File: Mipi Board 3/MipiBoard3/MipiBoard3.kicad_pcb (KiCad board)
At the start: 4 copper layers, 55 x 45 mm, 21 parts, among them J1 Power/Control Top, J2 Bank A Top, J3 Bank B Top, J4 MIPI1, J5 MIPI2, J6 Bank A Bottom, J7 Bank B Bottom, J8 Power/Control Bottom

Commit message: Components layedout
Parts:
- added C1: C, Capacitor_SMD:C_0201_0603Metric, F.Cu at (77.6, 60.2)
- added C2: C, Capacitor_SMD:C_0201_0603Metric, F.Cu at (77.7, 67.6)
- added C3: C, Capacitor_SMD:C_0201_0603Metric, F.Cu at (77.6, 75.0)
- added C4: C, Capacitor_SMD:C_0201_0603Metric, F.Cu at (65.6, 60.0)
- added R14: R, Resistor_SMD:R_0603_1608Metric, F.Cu at (65.6, 58.7)
- added R15: R, Resistor_SMD:R_0603_1608Metric, F.Cu at (62.4, 58.7)
- added R16: R, Resistor_SMD:R_0402_1005Metric, F.Cu at (71.4, 65.8)
- added R17: R, Resistor_SMD:R_0402_1005Metric, F.Cu at (72.3, 73.2)
- added R18: R, Resistor_SMD:R_0402_1005Metric, F.Cu at (71.8, 80.5)
- added R19: R, Resistor_SMD:R_0402_1005Metric, F.Cu at (83.4, 80.0)
- added R20: R, Resistor_SMD:R_0402_1005Metric, F.Cu at (83.8, 72.6)
- added R21: R, Resistor_SMD:R_0402_1005Metric, F.Cu at (83.3, 65.2)
- added R22: R, Resistor_SMD:R_0402_1005Metric, F.Cu at (71.4, 64.5)
- added R23: R, Resistor_SMD:R_0402_1005Metric, F.Cu at (72.3, 71.9)
- added R24: R, Resistor_SMD:R_0402_1005Metric, F.Cu at (71.8, 79.3)
- added R25: R, Resistor_SMD:R_0603_1608Metric, F.Cu at (84.9, 77.3)
- added R26: R, Resistor_SMD:R_0603_1608Metric, F.Cu at (84.9, 75.8)
- added R27: R, Resistor_SMD:R_0603_1608Metric, F.Cu at (84.9, 69.9)
- added R28: R, Resistor_SMD:R_0603_1608Metric, F.Cu at (84.9, 68.4)
- added R29: R, Resistor_SMD:R_0603_1608Metric, F.Cu at (71.6, 62.5)
- added R30: R, Resistor_SMD:R_0603_1608Metric, F.Cu at (71.6, 60.8)
- added R31: R, Resistor_SMD:R_0603_1608Metric, F.Cu at (84.2, 62.0)
- added R32: R, Resistor_SMD:R_0603_1608Metric, F.Cu at (84.2, 60.3)
- added R33: R, Resistor_SMD:R_0603_1608Metric, F.Cu at (70.8, 68.3)
- added R34: R, Resistor_SMD:R_0603_1608Metric, F.Cu at (70.8, 70.1)
- added R35: R, Resistor_SMD:R_0603_1608Metric, F.Cu at (71.2, 76.2)
- added R36: R, Resistor_SMD:R_0603_1608Metric, F.Cu at (71.2, 77.7)
- added U1: LM339, Package_SO:TSSOP-14-1EP_4.4x5mm_P0.65mm, F.Cu at (77.8, 63.9)
- added U2: LM339, Package_SO:TSSOP-14-1EP_4.4x5mm_P0.65mm, F.Cu at (77.9, 71.2)
- added U3: LM339, Package_SO:TSSOP-14-1EP_4.4x5mm_P0.65mm, F.Cu at (77.8, 78.7)
- moved R7 34.3 mm to (59.7, 67.0), turned to 90 degrees
- moved R10 32.9 mm to (59.7, 70.0), turned to 90 degrees
- moved R13 32.4 mm to (59.7, 73.1), turned to 90 degrees
- moved R12 11.3 mm to (83.3, 63.9)
- moved R2 10.7 mm to (60.7, 79.9), turned to -90 degrees
- moved R9 8.86 mm to (83.7, 71.2)
- moved R6 8.75 mm to (83.5, 78.8)
- moved R1 5.14 mm to (63.0, 79.9), turned to -90 degrees
- moved R3 4.40 mm to (92.3, 64.4)
- moved R4 3.60 mm to (94.8, 64.4)
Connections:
- J4 pad 10: GND -> 34_L5/1.5B_P
- J4 pad 11: GND -> 34_L5/1.5B_N
- J4 pad 13: GND -> 34_L1/1.5B_P
- J4 pad 14: GND -> 34_L1/1.5B_N
- J4 pad 7: GND -> 34_L3/1.5B_P
- J4 pad 8: GND -> 34_L3/1.5B_N
- J5 pad 10: 34_L5/1.5B_P -> 34_L8/1.5B_P
- J5 pad 11: 34_L5/1.5B_N -> 34_L8/1.5B_N
- J5 pad 13: 34_L9/1.5B_P -> 34_L7/1.5B_P
- J5 pad 14: 34_L9/1.5B_N -> 34_L7/1.5B_N
- J5 pad 7: 34_L6/1.5B_P -> 34_L9/1.5B_P
- J5 pad 8: 34_L6/1.5B_N -> 34_L9/1.5B_N
- R10 pad 1: 34_L7/1.5B_N -> 34_L5/1.5B_P
- R11 pad 1: 34_L6/1.5B_P -> 34_L9/1.5B_P
- R11 pad 2: 34_L6/1.5B_N -> 34_L9/1.5B_N
- R12 pad 1: 34_L4/1.5B_P -> Net-(U1C-+)
- R12 pad 2: 34_L6/1.5B_P -> 34_L9/1.5B_P
- R13 pad 1: 34_L4/1.5B_N -> 34_L3/1.5B_P
- R13 pad 2: 34_L6/1.5B_N -> 34_L3/1.5B_N
- R5 pad 1: 34_L9/1.5B_P -> 34_L7/1.5B_P
- R5 pad 2: 34_L9/1.5B_N -> 34_L7/1.5B_N
- R6 pad 1: 34_L8/1.5B_P -> Net-(U3C-+)
- R6 pad 2: 34_L9/1.5B_P -> 34_L7/1.5B_P
- R7 pad 1: 34_L8/1.5B_N -> 34_L1/1.5B_P
- R7 pad 2: 34_L9/1.5B_N -> 34_L1/1.5B_N
- R8 pad 1: 34_L5/1.5B_P -> 34_L8/1.5B_P
- R8 pad 2: 34_L5/1.5B_N -> 34_L8/1.5B_N
- R9 pad 1: 34_L7/1.5B_P -> Net-(U2C-+)
- R9 pad 2: 34_L5/1.5B_P -> 34_L8/1.5B_P
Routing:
- net +3V3: track 81.3 -> 10.0 mm
- net 14_L10_N/1.2C: track 40.3 -> 1.72 mm, vias 3 -> 1
- net 14_L10_P/1.2C: track 37.9 -> 0.00 mm, vias 2 -> 0
- net 14_L15_N/1.2C: track 37.6 -> 1.97 mm
- net 14_L22_N/1.2D: track 37.6 -> 2.20 mm
- net 14_L22_P/1.2D: track 36.8 -> 2.17 mm
- net 34_L7/1.5B_P: track 33.5 -> 0.00 mm, vias 1 -> 0
- net 34_L6/1.5B_P: track 33.6 -> 0.79 mm
- net 14_L16_P/1.2C: track 34.6 -> 1.79 mm, vias 2 -> 1
- net 34_L9/1.5B_N: track 31.9 -> 0.00 mm, vias 2 -> 0
- net 34_L5/1.5B_P: track 34.0 -> 2.77 mm, vias 2 -> 1
- net 34_L5/1.5B_N: track 33.2 -> 2.01 mm, vias 2 -> 1
- net 34_L7/1.5B_N: track 31.1 -> 0.00 mm, vias 1 -> 0
- net 14_L16_N/1.2C: track 32.8 -> 1.72 mm
- net 34_L8/1.5B_N: track 31.1 -> 0.00 mm, vias 1 -> 0
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
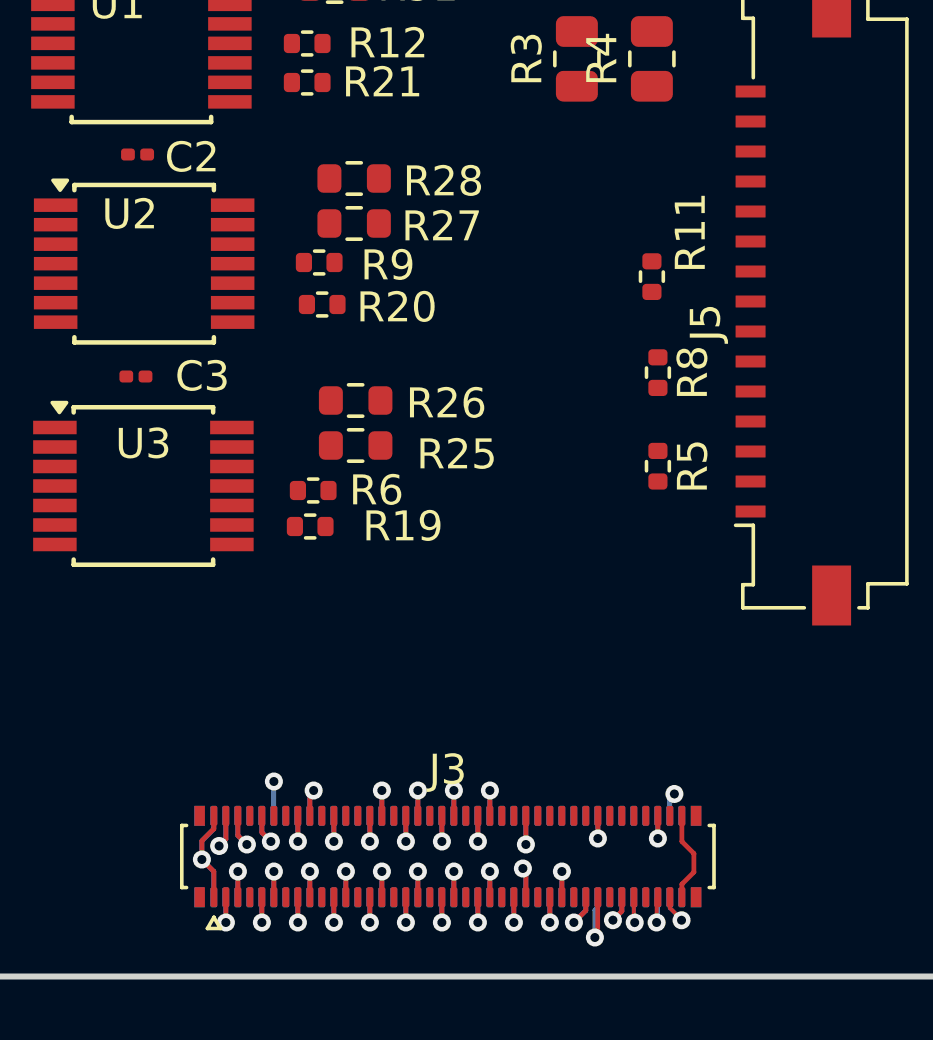
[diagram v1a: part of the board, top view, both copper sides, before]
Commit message: first few wires routed
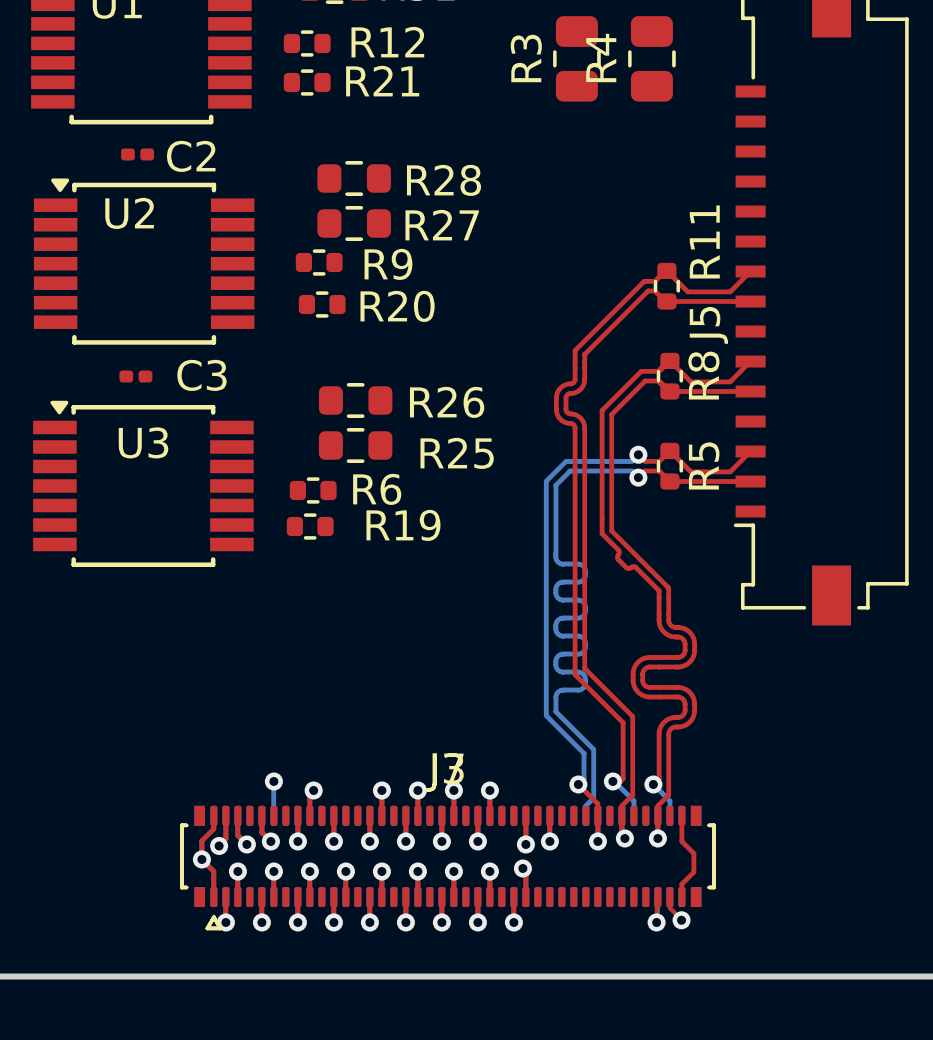
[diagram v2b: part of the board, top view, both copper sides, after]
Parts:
- moved R11 0.59 mm to (95.3, 72.0)
- moved R8 0.42 mm to (95.4, 75.0)
- moved R5 0.40 mm to (95.4, 78.0)
- moved J7 0.08 mm to (88.0, 91.0)
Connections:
- J4 pad 10: 34_L5/1.5B_P -> 34_L4/1.5B_P
- J4 pad 11: 34_L5/1.5B_N -> 34_L4/1.5B_N
- J4 pad 13: 34_L1/1.5B_P -> 34_L7/1.5B_P
- J4 pad 14: 34_L1/1.5B_N -> 34_L7/1.5B_N
- J5 pad 10: 34_L8/1.5B_P -> 34_L6/1.5B_P
- J5 pad 11: 34_L8/1.5B_N -> 34_L6/1.5B_N
- J5 pad 13: 34_L7/1.5B_P -> 34_L8/1.5B_P
- J5 pad 14: 34_L7/1.5B_N -> 34_L8/1.5B_N
- R10 pad 1: 34_L5/1.5B_P -> 34_L4/1.5B_P
- R10 pad 2: 34_L5/1.5B_N -> 34_L4/1.5B_N
- R16 pad 2: 34_L1/1.5B_P -> 34_L7/1.5B_P
- R17 pad 2: 34_L5/1.5B_P -> 34_L4/1.5B_P
- R19 pad 2: 34_L7/1.5B_N -> 34_L8/1.5B_N
- R20 pad 2: 34_L8/1.5B_N -> 34_L6/1.5B_N
- R22 pad 2: 34_L1/1.5B_N -> 34_L7/1.5B_N
- R23 pad 2: 34_L5/1.5B_N -> 34_L4/1.5B_N
- R5 pad 1: 34_L7/1.5B_P -> 34_L8/1.5B_P
- R5 pad 2: 34_L7/1.5B_N -> 34_L8/1.5B_N
- R6 pad 2: 34_L7/1.5B_P -> 34_L8/1.5B_P
- R7 pad 1: 34_L1/1.5B_P -> 34_L7/1.5B_P
- R7 pad 2: 34_L1/1.5B_N -> 34_L7/1.5B_N
- R8 pad 1: 34_L8/1.5B_P -> 34_L6/1.5B_P
- R8 pad 2: 34_L8/1.5B_N -> 34_L6/1.5B_N
- R9 pad 2: 34_L8/1.5B_P -> 34_L6/1.5B_P
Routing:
- net 34_L9/1.5B_N: track 0.00 -> 25.0 mm, vias 0 -> 1
- net 34_L9/1.5B_P: track 0.00 -> 25.0 mm, vias 0 -> 1
- net 34_L8/1.5B_N: track 0.00 -> 24.7 mm, vias 0 -> 1
- net 34_L6/1.5B_P: track 0.79 -> 25.2 mm
- net 34_L6/1.5B_N: track 1.52 -> 25.3 mm
- net 34_L8/1.5B_P: track 1.52 -> 21.7 mm, vias 1 -> 3
- net 34_L5/1.5B_P: track 2.77 -> 0.00 mm, vias 1 -> 0
- net 34_L5/1.5B_N: track 2.01 -> 0.00 mm, vias 1 -> 0
- net 34_L1_N/1.5A: track 1.78 -> 0.00 mm, vias 1 -> 0
- net 34_L3/1.5B_P: track 1.72 -> 0.00 mm, vias 1 -> 0
- net 34_L1_P/1.5A: track 1.72 -> 0.00 mm, vias 1 -> 0
- net 34_L7/1.5B_N: track 0.00 -> 1.72 mm, vias 0 -> 1
- net 34_L3/1.5B_N: track 1.68 -> 0.00 mm, vias 1 -> 0

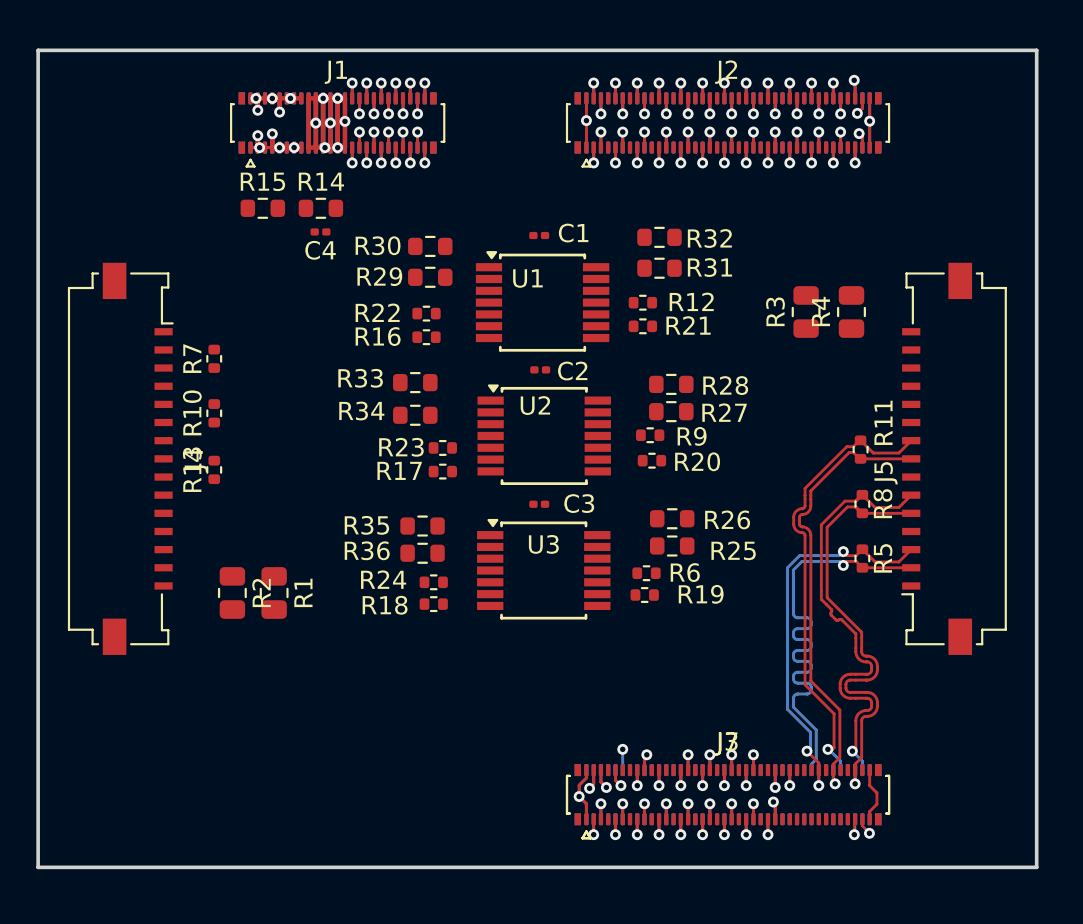
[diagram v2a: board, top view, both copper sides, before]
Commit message: length pairs matching
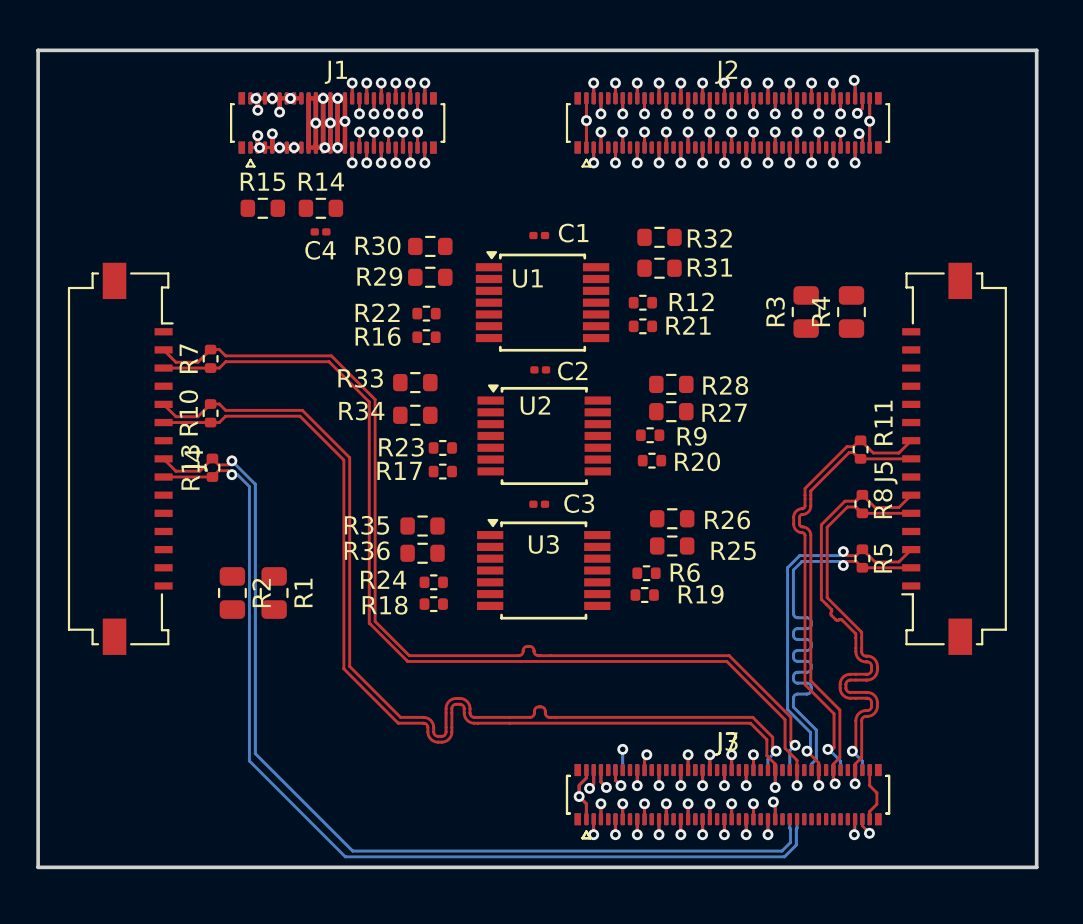
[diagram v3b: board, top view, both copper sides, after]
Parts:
- moved R10 0.20 mm to (59.5, 70.0)
- moved R7 0.20 mm to (59.5, 67.0)
- moved R13 0.16 mm to (59.6, 73.0)
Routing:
- net 34_L7/1.5B_P: track 0.00 -> 54.4 mm, vias 0 -> 1
- net 34_L3/1.5B_N: track 0.00 -> 54.4 mm, vias 0 -> 1
- net 34_L3/1.5B_P: track 0.00 -> 54.4 mm, vias 0 -> 1
- net 34_L4/1.5B_N: track 0.01 -> 54.3 mm, vias 0 -> 1
- net 34_L7/1.5B_N: track 1.72 -> 54.5 mm
- net 34_L4/1.5B_P: track 1.92 -> 54.3 mm

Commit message: better central wiring
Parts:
- moved R32 13.3 mm to (71.2, 62.7)
- moved R31 13.1 mm to (71.2, 61.1)
- moved R29 12.8 mm to (84.4, 62.6), turned to 180 degrees
- moved R30 12.7 mm to (84.3, 61.0), turned to 180 degrees
- moved R14 2.49 mm to (64.2, 60.8), turned to 90 degrees
- moved R15 2.03 mm to (62.5, 60.7), turned to -90 degrees
- moved R12 0.52 mm to (83.8, 64.1)
- moved R21 0.49 mm to (83.8, 65.3), turned to 0 degrees
- moved R34 0.38 mm to (71.1, 69.9)
- moved C4 0.33 mm to (65.4, 60.3), turned to -90 degrees
- moved R33 0.32 mm to (71.1, 68.3)
- moved R19 0.31 mm to (83.7, 80.1)
- moved C3 0.30 mm to (77.9, 75.0), turned to 0 degrees
- moved R9 0.22 mm to (83.8, 71.4)
- moved R6 0.21 mm to (83.7, 78.9)
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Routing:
- net +3V3: track 10.0 -> 154.9 mm
- net DividerVoltage: track 0.00 -> 81.2 mm, vias 0 -> 11
- net 14_L17_N/1.2C: track 1.68 -> 26.9 mm, vias 1 -> 2
- net 14_L9_N/1.2C: track 1.72 -> 26.7 mm, vias 1 -> 2
- net 14_L9_P/1.2B: track 1.69 -> 25.4 mm, vias 1 -> 2
- net 14_L17_P/1.2C: track 1.72 -> 25.3 mm, vias 1 -> 2
- net 34_L8/1.5B_N: track 24.7 -> 42.6 mm, vias 1 -> 3
- net 14_L7_N/1.2B: track 1.72 -> 19.5 mm, vias 1 -> 2
- net 35_K5_SDA/1.4D: track 1.68 -> 19.3 mm, vias 1 -> 2
- net 14_L11_SRCC_P/1.2C: track 1.69 -> 18.0 mm, vias 1 -> 2
- net 35_E6_SCL/1.4A: track 1.72 -> 17.5 mm, vias 1 -> 2
- net GND: track 67.4 -> 81.7 mm, vias 10 -> 29
- net 34_L9/1.5B_N: track 25.0 -> 39.0 mm, vias 1 -> 3
- net 34_L9/1.5B_P: track 25.0 -> 38.5 mm, vias 1 -> 3
- net 34_L3/1.5B_P: track 54.4 -> 66.8 mm, vias 1 -> 4
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
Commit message: Finished wiring
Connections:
- J4 pad 2: 14_L15_P/1.2C -> 14_L21_N/1.2D
- J4 pad 3: 14_L15_N/1.2C -> 14_L21_P/1.2D
- J4 pad 4: 14_L22_P/1.2D -> 14_L17_N/1.2C
- J4 pad 5: 14_L22_N/1.2D -> 14_L17_P/1.2C
- J5 pad 2: 14_L10_P/1.2C -> 35_K5_SDA/1.4D
- J5 pad 3: 14_L10_N/1.2C -> 35_E6_SCL/1.4A
- J5 pad 4: 14_L16_P/1.2C -> 14_L14_SRCC_N/1.2C
- J5 pad 5: 14_L16_N/1.2C -> 14_L14_SRCC_P/1.2C
- R1 pad 1: 14_L15_N/1.2C -> 14_L21_P/1.2D
- R2 pad 1: 14_L15_P/1.2C -> 14_L21_N/1.2D
- R25 pad 2: 14_L7_P/1.2B -> D10_1V35/7.1B
- R26 pad 2: 14_L11_SRCC_N/1.2C -> D9_1V35/7.1B
- R28 pad 2: 14_L7_N/1.2B -> 14_L11_SRCC_N/1.2C
- R29 pad 2: 14_L9_P/1.2B -> 14_L7_P/1.2B
- R3 pad 1: 14_L10_N/1.2C -> 35_E6_SCL/1.4A
- R30 pad 2: 14_L9_N/1.2C -> 14_L7_N/1.2B
- R31 pad 2: 14_L17_N/1.2C -> 14_L9_P/1.2B
- R32 pad 2: 14_L17_P/1.2C -> 14_L9_N/1.2C
- R33 pad 2: 35_K5_SDA/1.4D -> 14_L15_P/1.2C
- R34 pad 2: 35_E6_SCL/1.4A -> 14_L15_N/1.2C
- R35 pad 2: 14_L14_SRCC_N/1.2C -> 14_L22_P/1.2D
- R36 pad 2: 14_L14_SRCC_P/1.2C -> 14_L22_N/1.2D
- R4 pad 1: 14_L10_P/1.2C -> 35_K5_SDA/1.4D
- U1 pad 1: 14_L17_N/1.2C -> 14_L9_P/1.2B
- U1 pad 13: 14_L9_P/1.2B -> 14_L7_P/1.2B
- U1 pad 14: 14_L9_N/1.2C -> 14_L7_N/1.2B
- U1 pad 2: 14_L17_P/1.2C -> 14_L9_N/1.2C
- U2 pad 1: 35_K5_SDA/1.4D -> 14_L15_P/1.2C
- U2 pad 14: 14_L7_N/1.2B -> 14_L11_SRCC_N/1.2C
- U2 pad 2: 35_E6_SCL/1.4A -> 14_L15_N/1.2C
- U3 pad 1: 14_L14_SRCC_N/1.2C -> 14_L22_P/1.2D
- U3 pad 13: 14_L7_P/1.2B -> D10_1V35/7.1B
- U3 pad 14: 14_L11_SRCC_N/1.2C -> D9_1V35/7.1B
- U3 pad 2: 14_L14_SRCC_P/1.2C -> 14_L22_N/1.2D
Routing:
- net 14_L21_P/1.2D: track 1.72 -> 44.8 mm, vias 1 -> 3
- net 14_L21_N/1.2D: track 1.68 -> 40.1 mm, vias 1 -> 3
- net 35_E6_SCL/1.4A: track 17.5 -> 51.2 mm, vias 2 -> 1
- net 35_K5_SDA/1.4D: track 19.3 -> 50.3 mm, vias 2 -> 1
- net 14_L14_SRCC_N/1.2C: track 12.6 -> 41.9 mm
- net 14_L14_SRCC_P/1.2C: track 11.7 -> 39.8 mm
- net 14_L7_P/1.2B: track 10.9 -> 38.4 mm, vias 1 -> 2
- net 14_L17_P/1.2C: track 25.3 -> 50.7 mm, vias 2 -> 3
- net 14_L15_P/1.2C: track 5.13 -> 29.9 mm, vias 1 -> 2
- net D9_1V35/7.1B: track 1.72 -> 26.3 mm, vias 1 -> 2
- net D10_1V35/7.1B: track 1.69 -> 24.9 mm, vias 1 -> 2
- net 14_L11_SRCC_N/1.2C: track 12.5 -> 33.5 mm, vias 1 -> 2
- net 14_L7_N/1.2B: track 19.5 -> 39.9 mm
- net 14_L17_N/1.2C: track 26.9 -> 47.2 mm, vias 2 -> 3
- net 14_L15_N/1.2C: track 8.67 -> 28.4 mm, vias 1 -> 2
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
